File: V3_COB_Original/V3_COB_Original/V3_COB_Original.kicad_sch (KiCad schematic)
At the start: 4 parts, among them J101 Conn_02x35_Counter_Clockwise_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

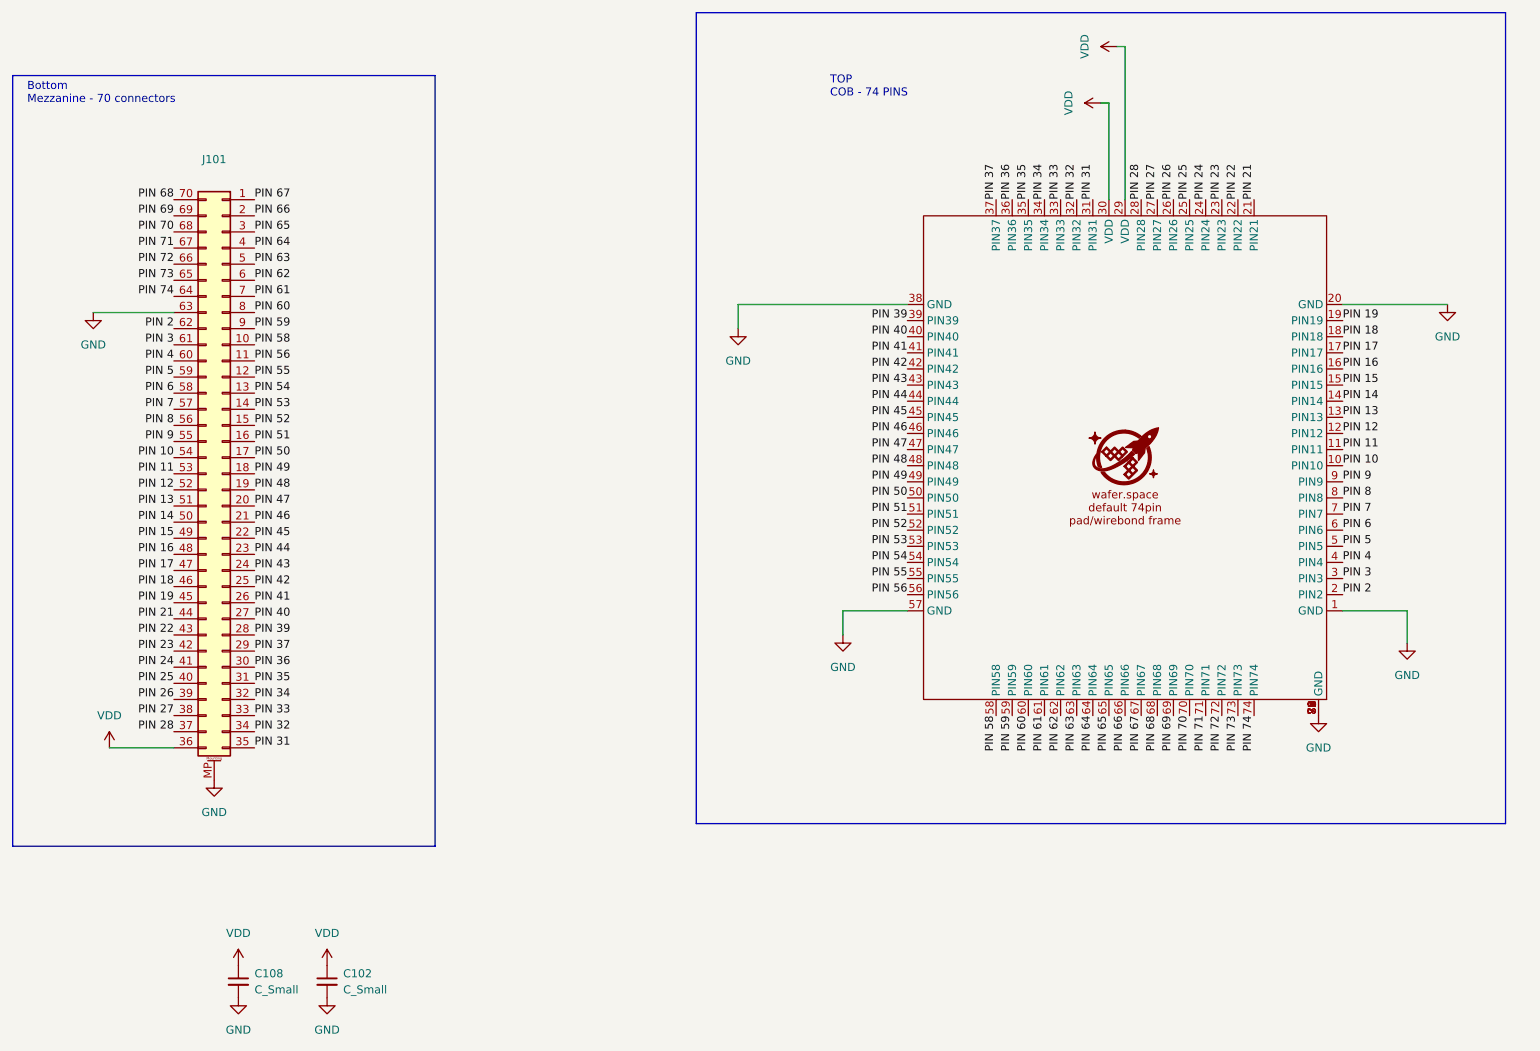
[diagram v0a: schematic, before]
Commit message: xp re-route the wire for original design to make chip in correct direction
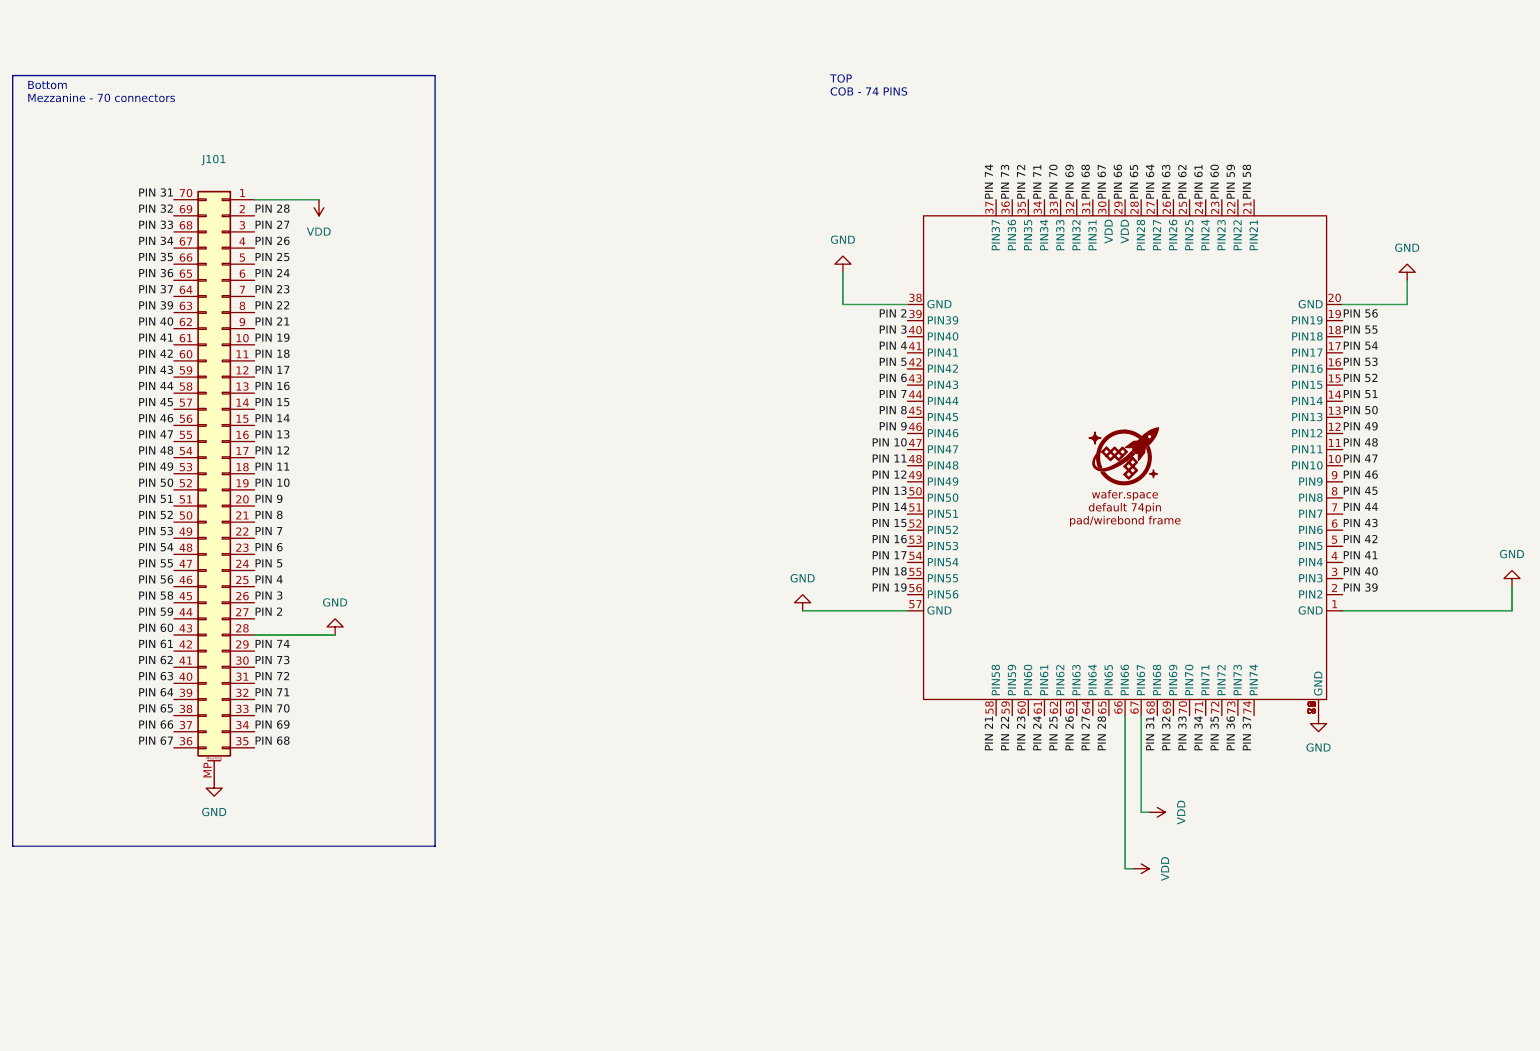
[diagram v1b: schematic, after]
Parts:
- removed C102, C108: C_Small, Capacitor_SMD:C_0201_0603Metric, symbol Device:C_Small
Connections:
- net GND: now also J101.28 (Pin_28); no longer J101.63 (Pin_63)
- net PIN 10: now also J101.19 (Pin_19), U102.47 (PIN47); no longer J101.54 (Pin_54), U102.10 (PIN10)
- net PIN 11: now also J101.18 (Pin_18), U102.48 (PIN48); no longer J101.53 (Pin_53), U102.11 (PIN11)
- net PIN 12: now also J101.17 (Pin_17), U102.49 (PIN49); no longer J101.52 (Pin_52), U102.12 (PIN12)
- net PIN 13: now also J101.16 (Pin_16), U102.50 (PIN50); no longer J101.51 (Pin_51), U102.13 (PIN13)
- net PIN 14: now also J101.15 (Pin_15), U102.51 (PIN51); no longer J101.50 (Pin_50), U102.14 (PIN14)
- net PIN 15: now also J101.14 (Pin_14), U102.52 (PIN52); no longer J101.49 (Pin_49), U102.15 (PIN15)
- net PIN 16: now also J101.13 (Pin_13), U102.53 (PIN53); no longer J101.48 (Pin_48), U102.16 (PIN16)
- net PIN 17: now also J101.12 (Pin_12), U102.54 (PIN54); no longer J101.47 (Pin_47), U102.17 (PIN17)
- net PIN 18: now also J101.11 (Pin_11), U102.55 (PIN55); no longer J101.46 (Pin_46), U102.18 (PIN18)
- net PIN 19: now also J101.10 (Pin_10), U102.56 (PIN56); no longer J101.45 (Pin_45), U102.19 (PIN19)
- net PIN 2: now also J101.27 (Pin_27), U102.39 (PIN39); no longer J101.62 (Pin_62), U102.2 (PIN2)
- net PIN 21: now also J101.9 (Pin_9), U102.58 (PIN58); no longer J101.44 (Pin_44), U102.21 (PIN21)
- net PIN 22: now also J101.8 (Pin_8), U102.59 (PIN59); no longer J101.43 (Pin_43), U102.22 (PIN22)
- net PIN 23: now also J101.7 (Pin_7), U102.60 (PIN60); no longer J101.42 (Pin_42), U102.23 (PIN23)
- net PIN 24: now also J101.6 (Pin_6), U102.61 (PIN61); no longer J101.41 (Pin_41), U102.24 (PIN24)
- net PIN 25: now also J101.5 (Pin_5), U102.62 (PIN62); no longer J101.40 (Pin_40), U102.25 (PIN25)
- net PIN 26: now also J101.4 (Pin_4), U102.63 (PIN63); no longer J101.39 (Pin_39), U102.26 (PIN26)
- net PIN 27: now also J101.3 (Pin_3), U102.64 (PIN64); no longer J101.38 (Pin_38), U102.27 (PIN27)
- net PIN 28: now also J101.2 (Pin_2), U102.65 (PIN65); no longer J101.37 (Pin_37), U102.28 (PIN28)
- net PIN 3: now also J101.26 (Pin_26), U102.40 (PIN40); no longer J101.61 (Pin_61), U102.3 (PIN3)
- net PIN 31: now also J101.70 (Pin_70), U102.68 (PIN68); no longer J101.35 (Pin_35), U102.31 (PIN31)
- net PIN 32: now also J101.69 (Pin_69), U102.69 (PIN69); no longer J101.34 (Pin_34), U102.32 (PIN32)
- net PIN 33: now also J101.68 (Pin_68), U102.70 (PIN70); no longer J101.33 (Pin_33), U102.33 (PIN33)
- net PIN 34: now also J101.67 (Pin_67), U102.71 (PIN71); no longer J101.32 (Pin_32), U102.34 (PIN34)
- net PIN 35: now also J101.66 (Pin_66), U102.72 (PIN72); no longer J101.31 (Pin_31), U102.35 (PIN35)
- net PIN 36: now also J101.65 (Pin_65), U102.73 (PIN73); no longer J101.30 (Pin_30), U102.36 (PIN36)
- net PIN 37: now also J101.64 (Pin_64), U102.74 (PIN74); no longer J101.29 (Pin_29), U102.37 (PIN37)
- net PIN 39: now also J101.63 (Pin_63), U102.2 (PIN2); no longer J101.28 (Pin_28), U102.39 (PIN39)
- net PIN 4: now also J101.25 (Pin_25), U102.41 (PIN41); no longer J101.60 (Pin_60), U102.4 (PIN4)
- net PIN 40: now also J101.62 (Pin_62), U102.3 (PIN3); no longer J101.27 (Pin_27), U102.40 (PIN40)
- net PIN 41: now also J101.61 (Pin_61), U102.4 (PIN4); no longer J101.26 (Pin_26), U102.41 (PIN41)
- net PIN 42: now also J101.60 (Pin_60), U102.5 (PIN5); no longer J101.25 (Pin_25), U102.42 (PIN42)
- net PIN 43: now also J101.59 (Pin_59), U102.6 (PIN6); no longer J101.24 (Pin_24), U102.43 (PIN43)
- net PIN 44: now also J101.58 (Pin_58), U102.7 (PIN7); no longer J101.23 (Pin_23), U102.44 (PIN44)
- net PIN 45: now also J101.57 (Pin_57), U102.8 (PIN8); no longer J101.22 (Pin_22), U102.45 (PIN45)
- net PIN 46: now also J101.56 (Pin_56), U102.9 (PIN9); no longer J101.21 (Pin_21), U102.46 (PIN46)
- net PIN 47: now also J101.55 (Pin_55), U102.10 (PIN10); no longer J101.20 (Pin_20), U102.47 (PIN47)
- net PIN 48: now also J101.54 (Pin_54), U102.11 (PIN11); no longer J101.19 (Pin_19), U102.48 (PIN48)
- net PIN 49: now also J101.53 (Pin_53), U102.12 (PIN12); no longer J101.18 (Pin_18), U102.49 (PIN49)
- net PIN 5: now also J101.24 (Pin_24), U102.42 (PIN42); no longer J101.59 (Pin_59), U102.5 (PIN5)
- net PIN 50: now also J101.52 (Pin_52), U102.13 (PIN13); no longer J101.17 (Pin_17), U102.50 (PIN50)
- net PIN 51: now also J101.51 (Pin_51), U102.14 (PIN14); no longer J101.16 (Pin_16), U102.51 (PIN51)
- net PIN 52: now also J101.50 (Pin_50), U102.15 (PIN15); no longer J101.15 (Pin_15), U102.52 (PIN52)
- net PIN 53: now also J101.49 (Pin_49), U102.16 (PIN16); no longer J101.14 (Pin_14), U102.53 (PIN53)
- net PIN 54: now also J101.48 (Pin_48), U102.17 (PIN17); no longer J101.13 (Pin_13), U102.54 (PIN54)
- net PIN 55: now also J101.47 (Pin_47), U102.18 (PIN18); no longer J101.12 (Pin_12), U102.55 (PIN55)
- net PIN 56: now also J101.46 (Pin_46), U102.19 (PIN19); no longer J101.11 (Pin_11), U102.56 (PIN56)
- net PIN 58: now also J101.45 (Pin_45), U102.21 (PIN21); no longer J101.10 (Pin_10), U102.58 (PIN58)
- net PIN 59: now also J101.44 (Pin_44), U102.22 (PIN22); no longer J101.9 (Pin_9), U102.59 (PIN59)
- net PIN 6: now also J101.23 (Pin_23), U102.43 (PIN43); no longer J101.58 (Pin_58), U102.6 (PIN6)
- net PIN 60: now also J101.43 (Pin_43), U102.23 (PIN23); no longer J101.8 (Pin_8), U102.60 (PIN60)
- net PIN 61: now also J101.42 (Pin_42), U102.24 (PIN24); no longer J101.7 (Pin_7), U102.61 (PIN61)
- net PIN 62: now also J101.41 (Pin_41), U102.25 (PIN25); no longer J101.6 (Pin_6), U102.62 (PIN62)
- net PIN 63: now also J101.40 (Pin_40), U102.26 (PIN26); no longer J101.5 (Pin_5), U102.63 (PIN63)
- net PIN 64: now also J101.39 (Pin_39), U102.27 (PIN27); no longer J101.4 (Pin_4), U102.64 (PIN64)
- net PIN 65: now also J101.38 (Pin_38), U102.28 (PIN28); no longer J101.3 (Pin_3), U102.65 (PIN65)
- net PIN 66: now also J101.37 (Pin_37), U102.29 (VDD); no longer J101.2 (Pin_2), U102.66 (PIN66)
- net PIN 67: now also J101.36 (Pin_36), U102.30 (VDD); no longer J101.1 (Pin_1), U102.67 (PIN67)
- net PIN 68: now also J101.35 (Pin_35), U102.31 (PIN31); no longer J101.70 (Pin_70), U102.68 (PIN68)
- net PIN 69: now also J101.34 (Pin_34), U102.32 (PIN32); no longer J101.69 (Pin_69), U102.69 (PIN69)
- net PIN 7: now also J101.22 (Pin_22), U102.44 (PIN44); no longer J101.57 (Pin_57), U102.7 (PIN7)
- net PIN 70: now also J101.33 (Pin_33), U102.33 (PIN33); no longer J101.68 (Pin_68), U102.70 (PIN70)
- net PIN 71: now also J101.32 (Pin_32), U102.34 (PIN34); no longer J101.67 (Pin_67), U102.71 (PIN71)
- net PIN 72: now also J101.31 (Pin_31), U102.35 (PIN35); no longer J101.66 (Pin_66), U102.72 (PIN72)
- net PIN 73: now also J101.30 (Pin_30), U102.36 (PIN36); no longer J101.65 (Pin_65), U102.73 (PIN73)
- net PIN 74: now also J101.29 (Pin_29), U102.37 (PIN37); no longer J101.64 (Pin_64), U102.74 (PIN74)
- net PIN 8: now also J101.21 (Pin_21), U102.45 (PIN45); no longer J101.56 (Pin_56), U102.8 (PIN8)
- net PIN 9: now also J101.20 (Pin_20), U102.46 (PIN46); no longer J101.55 (Pin_55), U102.9 (PIN9)
- net VDD: now also J101.1 (Pin_1), U102.66 (PIN66), U102.67 (PIN67); no longer J101.36 (Pin_36), U102.29 (VDD), U102.30 (VDD)
